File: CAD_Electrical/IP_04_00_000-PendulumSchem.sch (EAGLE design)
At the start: 7 parts, among them M1 SERVO, M2 SERVO

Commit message: Pressure sensors wired on A0, A1
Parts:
- added U$3, U$4: PRESSURE_SENSOR, IPcustomDevices:PRESSURE_SENSOR
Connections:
- new net N$12: B1.A0(RX0), U$3.V_OUT
- new net N$13: B1.A1(TX0), U$4.V_OUT
- net +24V: no longer VALVE_MANIFOLD.3
- net +5V: now also U$3.VCC, U$4.VCC
- net GND: now also U$3.GND, U$4.GND
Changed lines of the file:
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@@
 <part name="GND2" library="supply1" library_urn="urn:adsk.eagle:library:371" deviceset="GND" device=""/>
 <part name="GND7" library="supply1" library_urn="urn:adsk.eagle:library:371" deviceset="GND" device=""/>
-<part name="SUPPLY1" library="supply2" library_urn="urn:adsk.eagle:library:372" deviceset="+24V" device=""/>
 <part name="SUPPLY2" library="supply2" library_urn="urn:adsk.eagle:library:372" deviceset="+24V" device=""/>
+<part name="U$3" library="IPcustomDevices" deviceset="PRESSURE_SENSOR" device=""/>
+<part name="U$4" library="IPcustomDevices" deviceset="PRESSURE_SENSOR" device=""/>
+<part name="GND8" library="supply1" library_urn="urn:adsk.eagle:library:371" deviceset="GND" device=""/>
+<part name="GND9" library="supply1" library_urn="urn:adsk.eagle:library:371" deviceset="GND" device=""/>
+<part name="P+6" library="supply1" library_urn="urn:adsk.eagle:library:371" deviceset="+5V" device=""/>
+<part name="P+7" library="supply1" library_urn="urn:adsk.eagle:library:371" deviceset="+5V" device=""/>
 </parts>
 <sheets>
@@
 <attribute name="VALUE" x="185.42" y="55.88" size="1.778" layer="96"/>
 </instance>
-<instance part="SUPPLY1" gate="+24V" x="187.96" y="83.82" smashed="yes" rot="R90">
-<attribute name="VALUE" x="184.785" y="81.28" size="1.778" layer="96" rot="R90"/>
-</instance>
 <instance part="SUPPLY2" gate="+24V" x="147.32" y="60.96" smashed="yes" rot="R90">
 <attribute name="VALUE" x="144.145" y="58.42" size="1.778" layer="96" rot="R90"/>
+</instance>
+<instance part="U$3" gate="G$1" x="63.5" y="0" smashed="yes" rot="R270">
+<attribute name="NAME" x="86.36" y="30.48" size="1.778" layer="95" rot="R270"/>
+<attribute name="VALUE" x="66.04" y="30.48" size="1.778" layer="96" rot="R270"/>
+</instance>
+<instance part="U$4" gate="G$1" x="96.52" y="-5.08" smashed="yes" rot="R270">
+<attribute name="NAME" x="119.38" y="25.4" size="1.778" layer="95" rot="R270"/>
+<attribute name="VALUE" x="99.06" y="25.4" size="1.778" layer="96" rot="R270"/>
+</instance>
+<instance part="GND8" gate="1" x="78.74" y="43.18" smashed="yes" rot="R270">
+<attribute name="VALUE" x="76.2" y="45.72" size="1.778" layer="96" rot="R270"/>
+</instance>
+<instance part="GND9" gate="1" x="111.76" y="35.56" smashed="yes" rot="R270">
+<attribute name="VALUE" x="109.22" y="38.1" size="1.778" layer="96" rot="R270"/>
+</instance>
+<instance part="P+6" gate="1" x="66.04" y="40.64" smashed="yes" rot="R90">
+<attribute name="VALUE" x="71.12" y="38.1" size="1.778" layer="96" rot="R180"/>
+</instance>
+<instance part="P+7" gate="1" x="99.06" y="33.02" smashed="yes" rot="R90">
+<attribute name="VALUE" x="104.14" y="30.48" size="1.778" layer="96" rot="R180"/>
 </instance>
 </instances>
@@
 <wire x1="187.96" y1="81.28" x2="195.58" y2="81.28" width="0.1524" layer="91"/>
 </segment>
+<segment>
+<pinref part="U$3" gate="G$1" pin="GND"/>
+<pinref part="GND8" gate="1" pin="GND"/>
+<wire x1="81.28" y1="35.56" x2="81.28" y2="43.18" width="0.1524" layer="91"/>
+</segment>
+<segment>
+<pinref part="U$4" gate="G$1" pin="GND"/>
+<pinref part="GND9" gate="1" pin="GND"/>
+<wire x1="114.3" y1="30.48" x2="114.3" y2="35.56" width="0.1524" layer="91"/>
+</segment>
 </net>
 <net name="+5V" class="0">
@@
 <pinref part="P+1" gate="1" pin="+5V"/>
 <wire x1="157.48" y1="144.78" x2="157.48" y2="149.86" width="0.1524" layer="91"/>
+</segment>
+<segment>
+<pinref part="U$3" gate="G$1" pin="VCC"/>
+<wire x1="78.74" y1="35.56" x2="78.74" y2="40.64" width="0.1524" layer="91"/>
+<pinref part="P+6" gate="1" pin="+5V"/>
+<wire x1="78.74" y1="40.64" x2="68.58" y2="40.64" width="0.1524" layer="91"/>
+</segment>
+<segment>
+<pinref part="U$4" gate="G$1" pin="VCC"/>
+<wire x1="111.76" y1="30.48" x2="111.76" y2="33.02" width="0.1524" layer="91"/>
+<pinref part="P+7" gate="1" pin="+5V"/>
+<wire x1="111.76" y1="33.02" x2="101.6" y2="33.02" width="0.1524" layer="91"/>
 </segment>
 </net>
@@
 <wire x1="149.86" y1="63.5" x2="149.86" y2="60.96" width="0.1524" layer="91"/>
 </segment>
-<segment>
-<pinref part="SUPPLY1" gate="+24V" pin="+24V"/>
-<pinref part="VALVE_MANIFOLD" gate="A" pin="3"/>
-<wire x1="190.5" y1="83.82" x2="195.58" y2="83.82" width="0.1524" layer="91"/>
-</segment>
 </net>
 <net name="N$6" class="0">
@@
 </segment>
 </net>
+<net name="N$12" class="0">
+<segment>
+<pinref part="U$3" gate="G$1" pin="V_OUT"/>
+<wire x1="83.82" y1="35.56" x2="83.82" y2="134.62" width="0.1524" layer="91"/>
+<pinref part="B1" gate="G$1" pin="A0(RX0)"/>
+<wire x1="83.82" y1="134.62" x2="88.9" y2="134.62" width="0.1524" layer="91"/>
+</segment>
+</net>
+<net name="N$13" class="0">
+<segment>
+<pinref part="U$4" gate="G$1" pin="V_OUT"/>
+<wire x1="116.84" y1="30.48" x2="116.84" y2="38.1" width="0.1524" layer="91"/>
+<wire x1="116.84" y1="38.1" x2="86.36" y2="38.1" width="0.1524" layer="91"/>
+<wire x1="86.36" y1="38.1" x2="86.36" y2="132.08" width="0.1524" layer="91"/>
+<pinref part="B1" gate="G$1" pin="A1(TX0)"/>
+<wire x1="86.36" y1="132.08" x2="88.9" y2="132.08" width="0.1524" layer="91"/>
+</segment>
+</net>

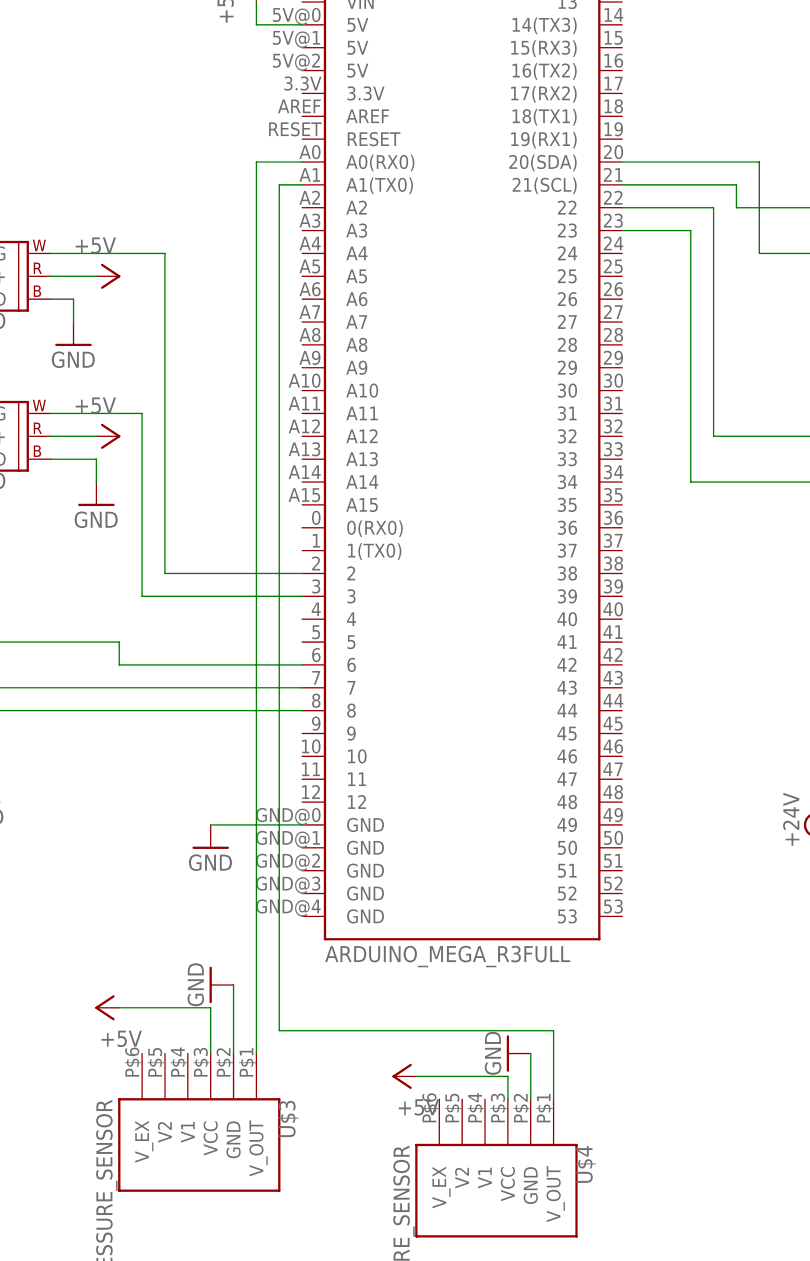
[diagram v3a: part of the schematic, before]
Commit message: Fixed analog pins away from dual serial pins for pressure sensors
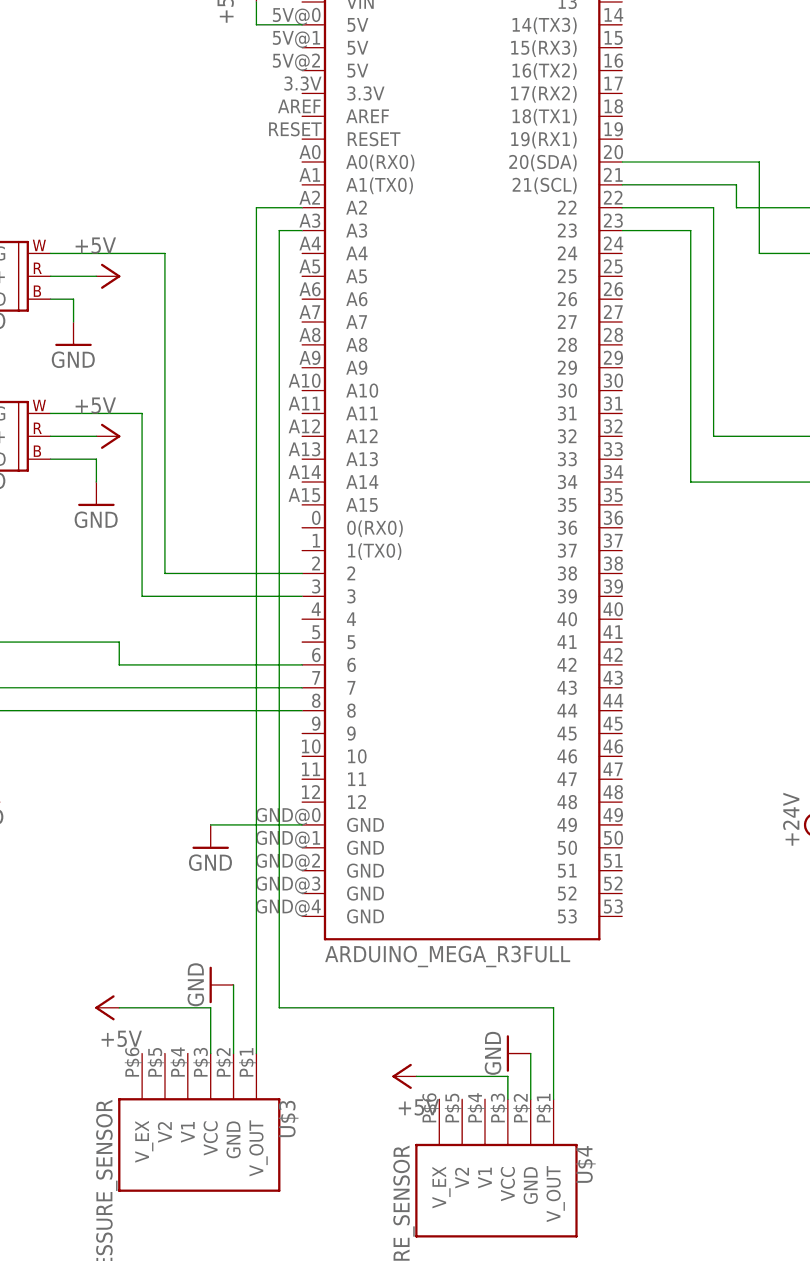
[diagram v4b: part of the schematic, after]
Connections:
- removed net N$13: B1.A1(TX0), U$4.V_OUT
- new net N$14: B1.A3, U$4.V_OUT
- net N$12: now also B1.A2; no longer B1.A0(RX0)
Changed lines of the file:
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@@
 <segment>
 <pinref part="U$3" gate="G$1" pin="V_OUT"/>
-<wire x1="83.82" y1="35.56" x2="83.82" y2="134.62" width="0.1524" layer="91"/>
-<pinref part="B1" gate="G$1" pin="A0(RX0)"/>
-<wire x1="83.82" y1="134.62" x2="88.9" y2="134.62" width="0.1524" layer="91"/>
+<wire x1="83.82" y1="35.56" x2="83.82" y2="129.54" width="0.1524" layer="91"/>
+<pinref part="B1" gate="G$1" pin="A2"/>
+<wire x1="83.82" y1="129.54" x2="88.9" y2="129.54" width="0.1524" layer="91"/>
 </segment>
 </net>
-<net name="N$13" class="0">
+<net name="N$14" class="0">
 <segment>
 <pinref part="U$4" gate="G$1" pin="V_OUT"/>
-<wire x1="116.84" y1="30.48" x2="116.84" y2="38.1" width="0.1524" layer="91"/>
-<wire x1="116.84" y1="38.1" x2="86.36" y2="38.1" width="0.1524" layer="91"/>
-<wire x1="86.36" y1="38.1" x2="86.36" y2="132.08" width="0.1524" layer="91"/>
-<pinref part="B1" gate="G$1" pin="A1(TX0)"/>
-<wire x1="86.36" y1="132.08" x2="88.9" y2="132.08" width="0.1524" layer="91"/>
+<wire x1="116.84" y1="30.48" x2="116.84" y2="40.64" width="0.1524" layer="91"/>
+<wire x1="116.84" y1="40.64" x2="86.36" y2="40.64" width="0.1524" layer="91"/>
+<pinref part="B1" gate="G$1" pin="A3"/>
+<wire x1="86.36" y1="40.64" x2="86.36" y2="127" width="0.1524" layer="91"/>
+<wire x1="86.36" y1="127" x2="88.9" y2="127" width="0.1524" layer="91"/>
 </segment>
 </net>

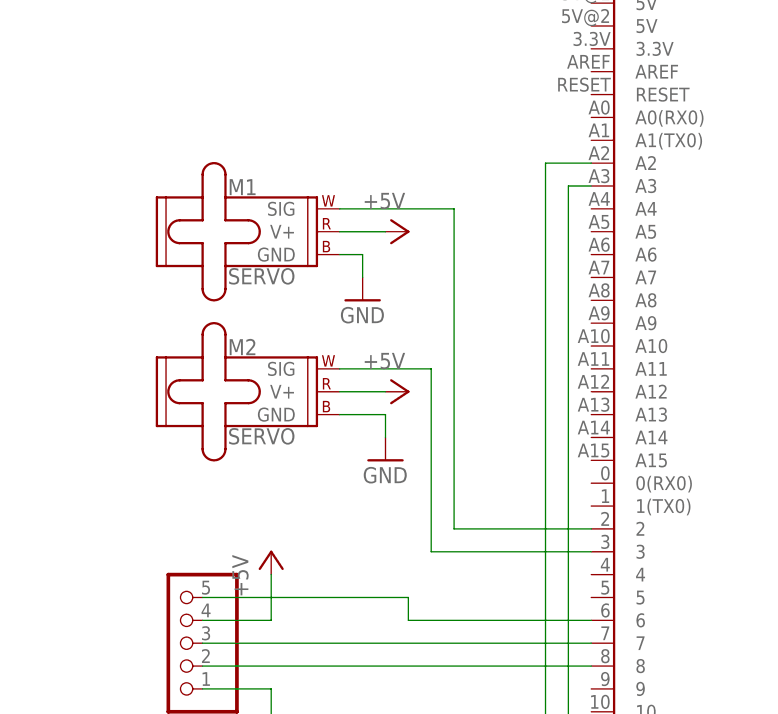
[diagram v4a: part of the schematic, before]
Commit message: Fixed footprints for each device
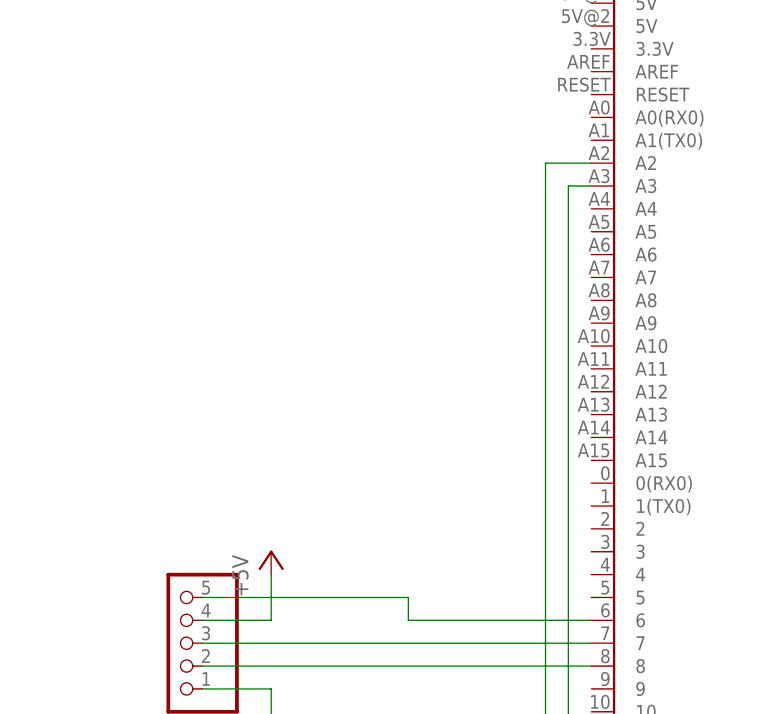
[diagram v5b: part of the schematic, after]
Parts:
- removed M1, M2: SERVO, SparkFun-Electromechanical:SERVO
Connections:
- removed net N$2: B1.3, M2.SIG
- removed net N$4: B1.2, M1.SIG
- net +5V: no longer M1.V+, M2.V+
- net GND: no longer M1.GND, M2.GND
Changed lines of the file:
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@@
 <part name="P+2" library="supply1" library_urn="urn:adsk.eagle:library:371" deviceset="+5V" device=""/>
 <part name="GND3" library="supply1" library_urn="urn:adsk.eagle:library:371" deviceset="GND" device=""/>
-<part name="M1" library="SparkFun-Electromechanical" library_urn="urn:adsk.eagle:library:516" deviceset="SERVO" device="" package3d_urn="urn:adsk.eagle:package:38562/1"/>
-<part name="M2" library="SparkFun-Electromechanical" library_urn="urn:adsk.eagle:library:516" deviceset="SERVO" device="" package3d_urn="urn:adsk.eagle:package:38562/1"/>
-<part name="GND4" library="supply1" library_urn="urn:adsk.eagle:library:371" deviceset="GND" device=""/>
-<part name="GND5" library="supply1" library_urn="urn:adsk.eagle:library:371" deviceset="GND" device=""/>
-<part name="P+3" library="supply1" library_urn="urn:adsk.eagle:library:371" deviceset="+5V" device=""/>
-<part name="P+4" library="supply1" library_urn="urn:adsk.eagle:library:371" deviceset="+5V" device=""/>
 <part name="ROTARY_ENCODER" library="pinhead" library_urn="urn:adsk.eagle:library:325" deviceset="PINHD-1X5" device="" package3d_urn="urn:adsk.eagle:package:22469/2"/>
 <part name="P+5" library="supply1" library_urn="urn:adsk.eagle:library:371" deviceset="+5V" device=""/>
@@
 <attribute name="VALUE" x="147.32" y="137.16" size="1.778" layer="96" rot="R270"/>
 </instance>
-<instance part="M1" gate="G$1" x="58.42" y="124.46" smashed="yes">
-<attribute name="NAME" x="48.514" y="125.984" size="1.778" layer="95" font="vector"/>
-<attribute name="VALUE" x="48.514" y="117.856" size="1.778" layer="95" font="vector" align="top-left"/>
-</instance>
-<instance part="M2" gate="G$1" x="58.42" y="106.68" smashed="yes">
-<attribute name="NAME" x="48.514" y="108.204" size="1.778" layer="95" font="vector"/>
-<attribute name="VALUE" x="48.514" y="100.076" size="1.778" layer="95" font="vector" align="top-left"/>
-</instance>
-<instance part="GND4" gate="1" x="63.5" y="114.3" smashed="yes">
-<attribute name="VALUE" x="60.96" y="111.76" size="1.778" layer="96"/>
-</instance>
-<instance part="GND5" gate="1" x="66.04" y="96.52" smashed="yes">
-<attribute name="VALUE" x="63.5" y="93.98" size="1.778" layer="96"/>
-</instance>
-<instance part="P+3" gate="1" x="68.58" y="121.92" smashed="yes" rot="R270">
-<attribute name="VALUE" x="63.5" y="124.46" size="1.778" layer="96"/>
-</instance>
-<instance part="P+4" gate="1" x="68.58" y="104.14" smashed="yes" rot="R270">
-<attribute name="VALUE" x="63.5" y="106.68" size="1.778" layer="96"/>
-</instance>
 <instance part="ROTARY_ENCODER" gate="A" x="43.18" y="76.2" smashed="yes" rot="R180">
 <attribute name="NAME" x="49.53" y="67.945" size="1.778" layer="95" rot="R180"/>
@@
 </segment>
 <segment>
-<pinref part="M2" gate="G$1" pin="GND"/>
-<wire x1="60.96" y1="101.6" x2="66.04" y2="101.6" width="0.1524" layer="91"/>
-<pinref part="GND5" gate="1" pin="GND"/>
-<wire x1="66.04" y1="101.6" x2="66.04" y2="99.06" width="0.1524" layer="91"/>
-</segment>
-<segment>
 <pinref part="ROTARY_ENCODER" gate="A" pin="1"/>
 <wire x1="45.72" y1="71.12" x2="53.34" y2="71.12" width="0.1524" layer="91"/>
@@
 </segment>
 <segment>
-<pinref part="M1" gate="G$1" pin="GND"/>
-<wire x1="60.96" y1="119.38" x2="63.5" y2="119.38" width="0.1524" layer="91"/>
-<pinref part="GND4" gate="1" pin="GND"/>
-<wire x1="63.5" y1="119.38" x2="63.5" y2="116.84" width="0.1524" layer="91"/>
-</segment>
-<segment>
 <pinref part="U$2" gate="G$1" pin="GND"/>
 <wire x1="177.8" y1="63.5" x2="187.96" y2="63.5" width="0.1524" layer="91"/>
@@
 <wire x1="88.9" y1="149.86" x2="83.82" y2="149.86" width="0.1524" layer="91"/>
 <wire x1="83.82" y1="149.86" x2="83.82" y2="152.4" width="0.1524" layer="91"/>
-</segment>
-<segment>
-<pinref part="P+3" gate="1" pin="+5V"/>
-<wire x1="60.96" y1="121.92" x2="66.04" y2="121.92" width="0.1524" layer="91"/>
-<pinref part="M1" gate="G$1" pin="V+"/>
-</segment>
-<segment>
-<pinref part="P+4" gate="1" pin="+5V"/>
-<wire x1="60.96" y1="104.14" x2="66.04" y2="104.14" width="0.1524" layer="91"/>
-<pinref part="M2" gate="G$1" pin="V+"/>
 </segment>
 <segment>
@@
 </segment>
 </net>
-<net name="N$4" class="0">
-<segment>
-<pinref part="M1" gate="G$1" pin="SIG"/>
-<wire x1="60.96" y1="124.46" x2="73.66" y2="124.46" width="0.1524" layer="91"/>
-<wire x1="73.66" y1="124.46" x2="73.66" y2="88.9" width="0.1524" layer="91"/>
-<pinref part="B1" gate="G$1" pin="2"/>
-<wire x1="73.66" y1="88.9" x2="88.9" y2="88.9" width="0.1524" layer="91"/>
-</segment>
-</net>
-<net name="N$2" class="0">
-<segment>
-<pinref part="M2" gate="G$1" pin="SIG"/>
-<wire x1="60.96" y1="106.68" x2="71.12" y2="106.68" width="0.1524" layer="91"/>
-<wire x1="71.12" y1="106.68" x2="71.12" y2="86.36" width="0.1524" layer="91"/>
-<pinref part="B1" gate="G$1" pin="3"/>
-<wire x1="71.12" y1="86.36" x2="88.9" y2="86.36" width="0.1524" layer="91"/>
-</segment>
-</net>
